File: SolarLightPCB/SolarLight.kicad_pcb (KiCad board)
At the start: 2 copper layers, 92 x 36.4 mm, 17 parts, among them J1 I2C, J2 SPI, SW1 Switch, SW2 ON_OFF, U1 TP4056, U2 WeMos_D1_mini

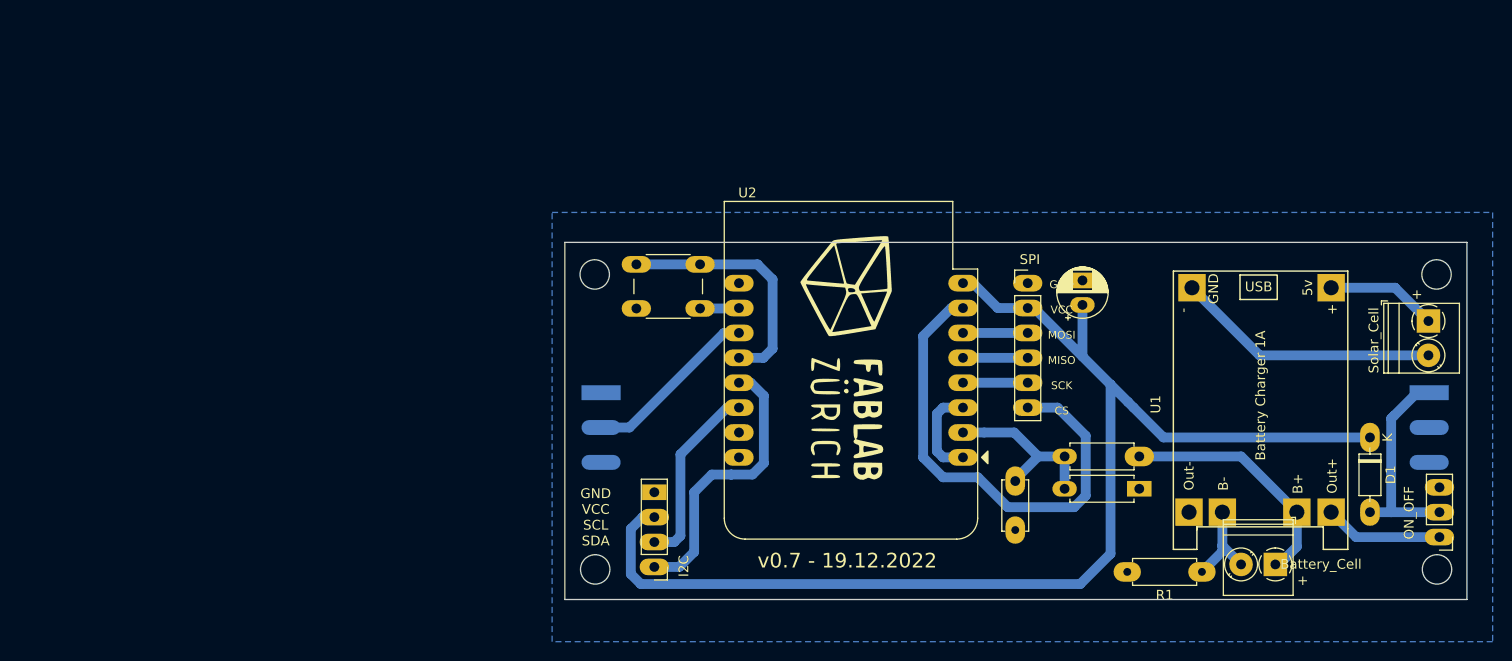
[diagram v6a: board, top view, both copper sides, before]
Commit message: Use the 5V to 3V3 regulator of the Wemos D1
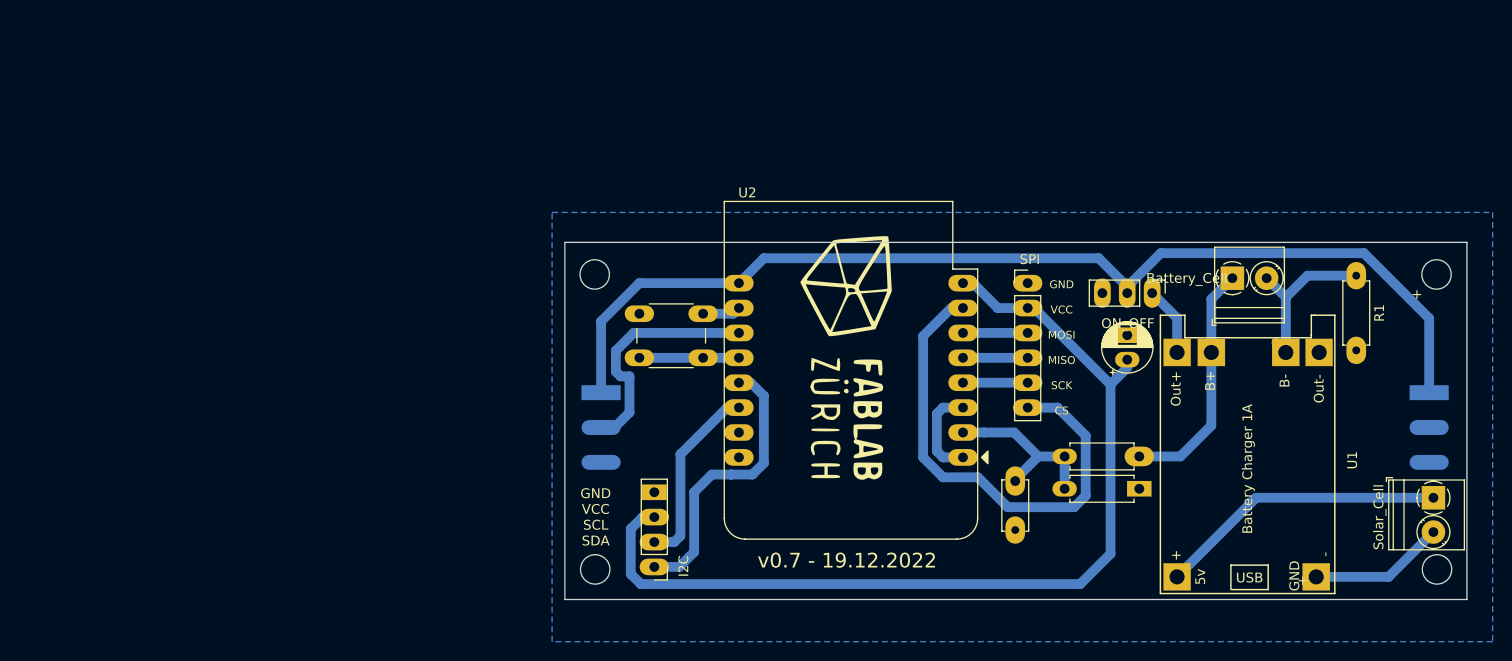
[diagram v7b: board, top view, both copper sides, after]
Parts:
- removed D1: 1N4148, Diode_THT:D_DO-35_SOD27_P7.62mm_Horizontal
- R2, R3: value R -> 140k
- moved JUMPER1 38.5 mm to (141.7, 65.5), turned to -90 degrees
- moved U1 38.1 mm to (142.6, 96.2), turned to 90 degrees
- moved R1 34.1 mm to (162.6, 63.8), turned to -90 degrees
- moved BT1 29.5 mm to (149.9, 64.0), turned to 0 degrees
- moved SC1 18.0 mm to (170.4, 86.4)
- moved SW1 11.7 mm to (95.9, 72.1), turned to 180 degrees
- moved C1 7.22 mm to (139.2, 72.3)
- renumbered SW2 to JUMPER1
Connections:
- net A0 renamed ADC
- net Net-(SW2-Pad1) renamed V_OUT
- JUMPER1 pad 2: /VNEO -> /5V
- LIN1 pad 1: /VNEO -> /5V
- LOUT1 pad 1: unconnected-(LOUT1-Pad1) -> /5V
- U2 pad 9: unconnected-(U2-Pad9) -> /5V
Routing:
- net /5V: track 0.00 -> 108.1 mm
- net +3V3: track 128.7 -> 98.0 mm
- net /VNEO: track 22.1 -> 0.00 mm
- net Net-(SC1-Pad1): track 11.3 -> 29.5 mm
- net SWITCH: track 25.4 -> 10.2 mm
- net Net-(SC1-Pad2): track 27.0 -> 13.9 mm
- net Net-(BT1-Pad2): track 9.66 -> 18.0 mm
- net Neopixel: track 18.1 -> 24.3 mm
- net V_OUT: track 12.1 -> 7.11 mm

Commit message: Remove the resistor for measuring the battery voltage even in the disconnected state
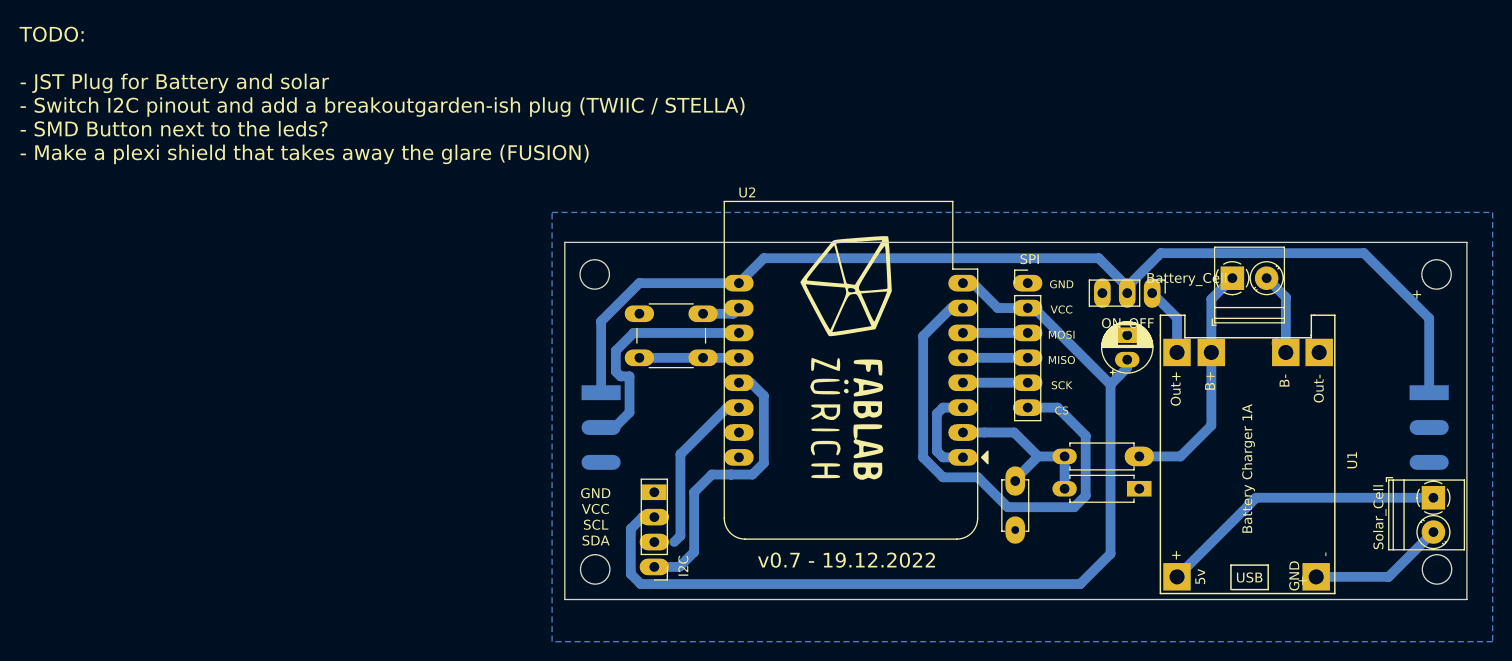
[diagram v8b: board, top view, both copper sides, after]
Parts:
- removed R1: 100k, Resistor_THT:R_Axial_DIN0207_L6.3mm_D2.5mm_P7.62mm_Horizontal
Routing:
- net Net-(BT1-Pad2): track 18.0 -> 9.76 mm
- net SCL: track 19.2 -> 17.2 mm
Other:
- board text added: "TODO: - JST Plug for Battery and solar - Switch I2C pinout and add a breakoutgarden-ish plug (TWIIC / STELLA) - SMD Button next to the leds? - Make a plexi shield that takes away the glare (FUSION)"
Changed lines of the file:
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@@
-    )
-  )
-  (footprint "Resistor_THT:R_Axial_DIN0207_L6.3mm_D2.5mm_P7.62mm_Horizontal" (layer "F.Cu")
-    (at 162.56 63.754 -90)
-    (descr "Resistor, Axial_DIN0207 series, Axial, Horizontal, pin pitch=7.62mm, 0.25W = 1/4W, length*diameter=6.3*2.5mm^2, http://cdn-reichelt.de/documents/datenblatt/B400/1_4W%23YAG.pdf")
-    (tags "Resistor Axial_DIN0207 series Axial Horizontal pin pitch 7.62mm 0.25W = 1/4W length 6.3mm diameter 2.5mm")
-    (property "Sheetfile" "SolarLight.kicad_sch")
-    (property "Sheetname" "")
-    (attr through_hole)
-    (fp_text reference "R1" (at 3.81 -2.37 90) (layer "F.SilkS")
-      (effects (font (size 1 1) (thickness 0.15)))
-    )
-    (fp_text value "100k" (at 3.81 2.37 90) (layer "F.Fab")
-      (effects (font (size 1 1) (thickness 0.15)))
-    )
-    (fp_text user "${REFERENCE}" (at 3.81 0 90) (layer "F.Fab")
-      (effects (font (size 1 1) (thickness 0.15)))
-    )
-    (fp_line (start 0.54 -1.04) (end 0.54 -1.37) (layer "F.SilkS") (width 0.12))
-    (fp_line (start 7.08 -1.37) (end 7.08 -1.04) (layer "F.SilkS") (width 0.12))
-    (fp_line (start 0.54 1.37) (end 7.08 1.37) (layer "F.SilkS") (width 0.12))
-    (fp_line (start 7.08 1.37) (end 7.08 1.04) (layer "F.SilkS") (width 0.12))
-    (fp_line (start 0.54 -1.37) (end 7.08 -1.37) (layer "F.SilkS") (width 0.12))
-    (fp_line (start 0.54 1.04) (end 0.54 1.37) (layer "F.SilkS") (width 0.12))
-    (fp_line (start 8.67 -1.5) (end -1.05 -1.5) (layer "F.CrtYd") (width 0.05))
-    (fp_line (start -1.05 1.5) (end 8.67 1.5) (layer "F.CrtYd") (width 0.05))
-    (fp_line (start 8.67 1.5) (end 8.67 -1.5) (layer "F.CrtYd") (width 0.05))
-    (fp_line (start -1.05 -1.5) (end -1.05 1.5) (layer "F.CrtYd") (width 0.05))
-    (fp_line (start 7.62 0) (end 6.96 0) (layer "F.Fab") (width 0.1))
-    (fp_line (start 6.96 1.25) (end 6.96 -1.25) (layer "F.Fab") (width 0.1))
-    (fp_line (start 0 0) (end 0.66 0) (layer "F.Fab") (width 0.1))
-    (fp_line (start 0.66 -1.25) (end 0.66 1.25) (layer "F.Fab") (width 0.1))
-    (fp_line (start 0.66 1.25) (end 6.96 1.25) (layer "F.Fab") (width 0.1))
-    (fp_line (start 6.96 -1.25) (end 0.66 -1.25) (layer "F.Fab") (width 0.1))
-    (pad "1" thru_hole oval (at 0 0 270) (size 2.8 2) (drill 0.8) (layers *.Cu *.Mask)
-      (net 19 "Net-(BT1-Pad2)") (pintype "passive"))
-    (pad "2" thru_hole oval (at 7.62 0 270) (size 2.8 2) (drill 0.8) (layers *.Cu *.Mask)
-      (net 2 "GND") (pintype "passive"))
-    (model "${KICAD6_3DMODEL_DIR}/Resistor_THT.3dshapes/R_Axial_DIN0207_L6.3mm_D2.5mm_P7.62mm_Horizontal.wrl"
-      (offset (xyz 0 0 0))
-      (scale (xyz 1 1 1))
-      (rotate (xyz 0 0 0))
     )
   )
@@
     (effects (font (size 0.8 0.8) (thickness 0.15)))
   )
+  (gr_text "TODO: \n\n- JST Plug for Battery and solar\n- Switch I2C pinout and add a breakoutgarden-ish plug (TWIIC / STELLA)\n- SMD Button next to the leds?\n- Make a plexi shield that takes away the glare (FUSION)" (at 26.162 45.212) (layer "F.SilkS")
+    (effects (font (size 1.5 1.5) (thickness 0.3)) (justify left))
+  )
   (gr_text "+" (at 168.75 65.65) (layer "F.SilkS")
     (effects (font (size 1 1) (thickness 0.15)))
@@
   (segment (start 99.568 77.216) (end 98.368 77.216) (width 1) (layer "B.Cu") (net 10))
   (segment (start 98.368 77.216) (end 93.596499 81.987501) (width 1) (layer "B.Cu") (net 10))
-  (segment (start 92.964 90.932) (end 90.932 90.932) (width 1) (layer "B.Cu") (net 10))
   (segment (start 93.596499 90.299501) (end 92.964 90.932) (width 1) (layer "B.Cu") (net 10))
   (segment (start 152.344 86.416) (end 144.272 94.488) (width 1) (layer "B.Cu") (net 14))
@@
   (segment (start 134.394 95.222) (end 137.485 92.131) (width 1) (layer "B.Cu") (net 18))
   (segment (start 139.192 72.325113) (end 139.192 73.152) (width 1) (layer "B.Cu") (net 18))
-  (segment (start 157.582 63.754) (end 162.56 63.754) (width 1) (layer "B.Cu") (net 19))
   (segment (start 153.416 64.008) (end 155.372 65.964) (width 1) (layer "B.Cu") (net 19))
   (segment (start 154.404 70.62) (end 155.372 71.588) (width 1) (layer "B.Cu") (net 19))
   (segment (start 155.372 65.964) (end 155.372 71.588) (width 1) (layer "B.Cu") (net 19))
-  (segment (start 155.372 65.964) (end 157.582 63.754) (width 1) (layer "B.Cu") (net 19))
-  (segment (start 162.498 63.816) (end 162.56 63.754) (width 1) (layer "B.Cu") (net 19))
   (segment (start 141.732 65.532) (end 144.272 68.072) (width 1) (layer "B.Cu") (net 20))
   (segment (start 144.272 68.072) (end 144.272 71.588) (width 1) (layer "B.Cu") (net 20))
